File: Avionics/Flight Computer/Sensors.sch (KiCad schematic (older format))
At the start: 11 parts, among them U5 MPU-9250, U7 LPS25HB

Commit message: Finished routing and DRC check.
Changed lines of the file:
@@
 $EndComp
 $Comp
-L GND #PWR0106
+L GND #PWR0122
 U 1 1 58B4AF5E
 P 2400 5300
-F 0 "#PWR0106" H -1950 1500 50  0001 C CNN
+F 0 "#PWR0122" H -1950 1500 50  0001 C CNN
 F 1 "GND" H 2405 5127 50  0000 C CNN
 F 2 "" H -1950 1750 50  0001 C CNN
@@
 $EndComp
 $Comp
-L +3.3V #PWR0107
+L +3.3V #PWR0123
 U 1 1 58B4AFA2
 P 2300 2850
-F 0 "#PWR0107" H -2200 -700 50  0001 C CNN
+F 0 "#PWR0123" H -2200 -700 50  0001 C CNN
 F 1 "+3.3V" H 2315 3023 50  0000 C CNN
 F 2 "" H -2200 -550 50  0001 C CNN
@@
 $EndComp
 $Comp
-L GND #PWR0108
+L GND #PWR0124
 U 1 1 58B4B105
 P 8400 3550
-F 0 "#PWR0108" H 4050 -250 50  0001 C CNN
+F 0 "#PWR0124" H 4050 -250 50  0001 C CNN
 F 1 "GND" H 8405 3377 50  0000 C CNN
 F 2 "" H 4050 0   50  0001 C CNN
@@
 Connection ~ 8400 3550
 $Comp
-L +3.3V #PWR0109
+L +3.3V #PWR0125
 U 1 1 58B4B14B
 P 8450 1900
-F 0 "#PWR0109" H 3950 -1650 50  0001 C CNN
+F 0 "#PWR0125" H 3950 -1650 50  0001 C CNN
 F 1 "+3.3V" H 8465 2073 50  0000 C CNN
 F 2 "" H 3950 -1500 50  0001 C CNN
@@
 Connection ~ 8450 2350
 $Comp
-L GND #PWR0110
+L GND #PWR0126
 U 1 1 58B4B9E9
 P 9050 2700
-F 0 "#PWR0110" H 4700 -1100 50  0001 C CNN
+F 0 "#PWR0126" H 4700 -1100 50  0001 C CNN
 F 1 "GND" H 9055 2527 50  0000 C CNN
 F 2 "" H 4700 -850 50  0001 C CNN
@@
 Wire Wire Line
 	8450 2250 8450 2350
-Text Notes 8750 2150 0    60   ~ 0
+Text Notes 8750 2000 0    60   ~ 0
 Input filter to reduce sensor reference noise. \n1.5kHz cutoff, 25uA bias current worst case
 $Comp
-L +3.3V #PWR0111
+L +3.3V #PWR0127
 U 1 1 58B4C158
 P 7450 2100
-F 0 "#PWR0111" H 2950 -1450 50  0001 C CNN
+F 0 "#PWR0127" H 2950 -1450 50  0001 C CNN
 F 1 "+3.3V" H 7465 2273 50  0000 C CNN
 F 2 "" H 2950 -1300 50  0001 C CNN
@@
 	3100 4500 3850 4500
 $Comp
-L GND #PWR0112
+L GND #PWR0128
 U 1 1 58B4FB3E
 P 3850 4800
-F 0 "#PWR0112" H -500 1000 50  0001 C CNN
+F 0 "#PWR0128" H -500 1000 50  0001 C CNN
 F 1 "GND" H 3855 4627 50  0000 C CNN
 F 2 "" H -500 1250 50  0001 C CNN
@@
 	3500 4800 3500 4750
 $Comp
-L +3.3V #PWR0113
+L +3.3V #PWR0129
 U 1 1 58B50137
 P 3500 4750
-F 0 "#PWR0113" H -1000 1200 50  0001 C CNN
+F 0 "#PWR0129" H -1000 1200 50  0001 C CNN
 F 1 "+3.3V" H 3515 4923 50  0000 C CNN
 F 2 "" H -1000 1350 50  0001 C CNN
@@
 IMU-INT
 $Comp
-L GND #PWR0114
+L GND #PWR0130
 U 1 1 58B505FC
 P 3350 3600
-F 0 "#PWR0114" H -1000 -200 50  0001 C CNN
+F 0 "#PWR0130" H -1000 -200 50  0001 C CNN
 F 1 "GND" H 3355 3427 50  0000 C CNN
 F 2 "" H -1000 50  50  0001 C CNN
@@
 	2500 3300 3350 3300
 Connection ~ 2500 3300
-Text Notes 2800 3150 0    60   ~ 0
+Text Notes 2600 2800 0    60   ~ 0
 Input filter to reduce sensor reference noise. \n33kHz cutoff, 3.5mA bias current worst case
 $Comp
-L GND #PWR0115
+L GND #PWR0131
 U 1 1 58B50B96
 P 1500 3600
-F 0 "#PWR0115" H -2850 -200 50  0001 C CNN
+F 0 "#PWR0131" H -2850 -200 50  0001 C CNN
 F 1 "GND" H 1505 3427 50  0000 C CNN
 F 2 "" H -2850 50  50  0001 C CNN
@@
 	8300 3550 8500 3550
 NoConn ~ 8000 3200
+$Comp
+L PWR_FLAG #FLG0132
+U 1 1 58BF1DC3
+P 3050 3300
+F 0 "#FLG0132" H -1800 125 50  0001 C CNN
+F 1 "PWR_FLAG" H 3050 3474 50  0000 C CNN
+F 2 "" H -1800 50  50  0001 C CNN
+F 3 "" H -1800 50  50  0001 C CNN
+	1    3050 3300
+	1    0    0    -1
+$EndComp
+Connection ~ 3050 3300
+$Comp
+L PWR_FLAG #FLG0133
+U 1 1 58BF1E5B
+P 8900 2350
+F 0 "#FLG0133" H 4050 -825 50  0001 C CNN
+F 1 "PWR_FLAG" H 8900 2524 50  0000 C CNN
+F 2 "" H 4050 -900 50  0001 C CNN
+F 3 "" H 4050 -900 50  0001 C CNN
+	1    8900 2350
+	1    0    0    -1
+$EndComp
+Connection ~ 8900 2350
 $EndSCHEMATC

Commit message: Added LEDs
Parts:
- removed U7: LPS25HB, Housings_LGA:HLGA-10L_2.5x2.5mm_Pitch0.6mm, symbol LPS25HB-RESCUE-Flight_Computer
- added U7: LPS25HB, Housings_LGA:HLGA-10L_2.5x2.5mm_Pitch0.6mm, symbol LPS25HB
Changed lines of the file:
@@
 EESchema Schematic File Version 2
-LIBS:Flight Computer-rescue
 LIBS:device
 LIBS:rfcom
@@
 $EndComp
 $Comp
-L GND #PWR0122
+L GND #PWR0130
 U 1 1 58B4AF5E
 P 2400 5300
-F 0 "#PWR0122" H -1950 1500 50  0001 C CNN
+F 0 "#PWR0130" H -1950 1500 50  0001 C CNN
 F 1 "GND" H 2405 5127 50  0000 C CNN
 F 2 "" H -1950 1750 50  0001 C CNN
@@
 $EndComp
 $Comp
-L +3.3V #PWR0123
+L +3.3V #PWR0131
 U 1 1 58B4AFA2
 P 2300 2850
-F 0 "#PWR0123" H -2200 -700 50  0001 C CNN
+F 0 "#PWR0131" H -2200 -700 50  0001 C CNN
 F 1 "+3.3V" H 2315 3023 50  0000 C CNN
 F 2 "" H -2200 -550 50  0001 C CNN
@@
 $EndComp
 $Comp
-L GND #PWR0124
+L GND #PWR0132
 U 1 1 58B4B105
 P 8400 3550
-F 0 "#PWR0124" H 4050 -250 50  0001 C CNN
+F 0 "#PWR0132" H 4050 -250 50  0001 C CNN
 F 1 "GND" H 8405 3377 50  0000 C CNN
 F 2 "" H 4050 0   50  0001 C CNN
@@
 Connection ~ 8400 3550
 $Comp
-L +3.3V #PWR0125
+L +3.3V #PWR0133
 U 1 1 58B4B14B
 P 8450 1900
-F 0 "#PWR0125" H 3950 -1650 50  0001 C CNN
+F 0 "#PWR0133" H 3950 -1650 50  0001 C CNN
 F 1 "+3.3V" H 8465 2073 50  0000 C CNN
 F 2 "" H 3950 -1500 50  0001 C CNN
@@
 Connection ~ 8450 2350
 $Comp
-L GND #PWR0126
+L GND #PWR0134
 U 1 1 58B4B9E9
 P 9050 2700
-F 0 "#PWR0126" H 4700 -1100 50  0001 C CNN
+F 0 "#PWR0134" H 4700 -1100 50  0001 C CNN
 F 1 "GND" H 9055 2527 50  0000 C CNN
 F 2 "" H 4700 -850 50  0001 C CNN
@@
 Input filter to reduce sensor reference noise. \n1.5kHz cutoff, 25uA bias current worst case
 $Comp
-L +3.3V #PWR0127
+L +3.3V #PWR0135
 U 1 1 58B4C158
 P 7450 2100
-F 0 "#PWR0127" H 2950 -1450 50  0001 C CNN
+F 0 "#PWR0135" H 2950 -1450 50  0001 C CNN
 F 1 "+3.3V" H 7465 2273 50  0000 C CNN
 F 2 "" H 2950 -1300 50  0001 C CNN
@@
 	3100 4500 3850 4500
 $Comp
-L GND #PWR0128
+L GND #PWR0136
 U 1 1 58B4FB3E
 P 3850 4800
-F 0 "#PWR0128" H -500 1000 50  0001 C CNN
+F 0 "#PWR0136" H -500 1000 50  0001 C CNN
 F 1 "GND" H 3855 4627 50  0000 C CNN
 F 2 "" H -500 1250 50  0001 C CNN
@@
 	3500 4800 3500 4750
 $Comp
-L +3.3V #PWR0129
+L +3.3V #PWR0137
 U 1 1 58B50137
 P 3500 4750
-F 0 "#PWR0129" H -1000 1200 50  0001 C CNN
+F 0 "#PWR0137" H -1000 1200 50  0001 C CNN
 F 1 "+3.3V" H 3515 4923 50  0000 C CNN
 F 2 "" H -1000 1350 50  0001 C CNN
@@
 IMU-INT
 $Comp
-L GND #PWR0130
+L GND #PWR0138
 U 1 1 58B505FC
 P 3350 3600
-F 0 "#PWR0130" H -1000 -200 50  0001 C CNN
+F 0 "#PWR0138" H -1000 -200 50  0001 C CNN
 F 1 "GND" H 3355 3427 50  0000 C CNN
 F 2 "" H -1000 50  50  0001 C CNN
@@
 Input filter to reduce sensor reference noise. \n33kHz cutoff, 3.5mA bias current worst case
 $Comp
-L GND #PWR0131
+L GND #PWR0139
 U 1 1 58B50B96
 P 1500 3600
-F 0 "#PWR0131" H -2850 -200 50  0001 C CNN
+F 0 "#PWR0139" H -2850 -200 50  0001 C CNN
 F 1 "GND" H 1505 3427 50  0000 C CNN
 F 2 "" H -2850 50  50  0001 C CNN
@@
 Text Notes 3900 4100 0    60   ~ 0
 AUX bus goes to connector for expansion sensors
-$Comp
-L LPS25HB-RESCUE-Flight_Computer U7
-U 1 1 58B3E15F
-P 8400 2950
-AR Path="/58B3E15F" Ref="U7"  Part="1"
-AR Path="/58AA09D0/58B3E15F" Ref="U7"  Part="1"
-F 0 "U7" H 8071 2996 50  0000 R CNN
-F 1 "LPS25HB" H 8071 2905 50  0000 R CNN
-F 2 "Housings_LGA:HLGA-10L_2.5x2.5mm_Pitch0.6mm" H -1250 700 50  0001 C CIN
-F 3 "http://www.st.com/resource/en/datasheet/lps25hb.pdf" H -1250 800 50  0001 C CNN
-	1    8400 2950
-	-1   0    0    -1
-$EndComp
 Text Notes 1000 5900 0    60   ~ 0
 Layout Note: Exposed pad is NC. Do not solder the exposed pad.
 Wire Wire Line
-	8300 3550 8500 3550
+	8300 3550 8600 3550
 NoConn ~ 8000 3200
 $Comp
-L PWR_FLAG #FLG0132
+L PWR_FLAG #FLG0140
 U 1 1 58BF1DC3
 P 3050 3300
-F 0 "#FLG0132" H -1800 125 50  0001 C CNN
+F 0 "#FLG0140" H -1800 125 50  0001 C CNN
 F 1 "PWR_FLAG" H 3050 3474 50  0000 C CNN
 F 2 "" H -1800 50  50  0001 C CNN
@@
 Connection ~ 3050 3300
 $Comp
-L PWR_FLAG #FLG0133
+L PWR_FLAG #FLG0141
 U 1 1 58BF1E5B
 P 8900 2350
-F 0 "#FLG0133" H 4050 -825 50  0001 C CNN
+F 0 "#FLG0141" H 4050 -825 50  0001 C CNN
 F 1 "PWR_FLAG" H 8900 2524 50  0000 C CNN
 F 2 "" H 4050 -900 50  0001 C CNN
@@
 $EndComp
 Connection ~ 8900 2350
+$Comp
+L LPS25HB U7
+U 1 1 58BE66D3
+P 8400 2950
+F 0 "U7" H 8071 2996 50  0000 R CNN
+F 1 "LPS25HB" H 8071 2905 50  0000 R CNN
+F 2 "Housings_LGA:HLGA-10L_2.5x2.5mm_Pitch0.6mm" H -1250 1100 50  0001 C CIN
+F 3 "http://www.st.com/resource/en/datasheet/lps25hb.pdf" H -1250 1200 50  0001 C CNN
+	1    8400 2950
+	-1   0    0    -1
+$EndComp
+Connection ~ 8500 3550
 $EndSCHEMATC

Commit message: Changed LED configuration, added smart driver chip to let all the CPUs access it..
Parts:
- C54, C55, C56, C58, R15, R16, R17, R18, R19: Voltage 50V -> 16V
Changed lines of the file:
@@
 $EndComp
 $Comp
-L GND #PWR0130
+L GND #PWR0134
 U 1 1 58B4AF5E
 P 2400 5300
-F 0 "#PWR0130" H -1950 1500 50  0001 C CNN
+F 0 "#PWR0134" H -1950 1500 50  0001 C CNN
 F 1 "GND" H 2405 5127 50  0000 C CNN
 F 2 "" H -1950 1750 50  0001 C CNN
@@
 $EndComp
 $Comp
-L +3.3V #PWR0131
+L +3.3V #PWR0135
 U 1 1 58B4AFA2
 P 2300 2850
-F 0 "#PWR0131" H -2200 -700 50  0001 C CNN
+F 0 "#PWR0135" H -2200 -700 50  0001 C CNN
 F 1 "+3.3V" H 2315 3023 50  0000 C CNN
 F 2 "" H -2200 -550 50  0001 C CNN
@@
 $EndComp
 $Comp
-L GND #PWR0132
+L GND #PWR0136
 U 1 1 58B4B105
 P 8400 3550
-F 0 "#PWR0132" H 4050 -250 50  0001 C CNN
+F 0 "#PWR0136" H 4050 -250 50  0001 C CNN
 F 1 "GND" H 8405 3377 50  0000 C CNN
 F 2 "" H 4050 0   50  0001 C CNN
@@
 Connection ~ 8400 3550
 $Comp
-L +3.3V #PWR0133
+L +3.3V #PWR0137
 U 1 1 58B4B14B
 P 8450 1900
-F 0 "#PWR0133" H 3950 -1650 50  0001 C CNN
+F 0 "#PWR0137" H 3950 -1650 50  0001 C CNN
 F 1 "+3.3V" H 8465 2073 50  0000 C CNN
 F 2 "" H 3950 -1500 50  0001 C CNN
@@
 F 2 "Capacitors_SMD:C_0402" H 2288 -1350 50  0001 C CNN
 F 3 "" H 2250 -1200 50  0001 C CNN
-F 4 "50V" H 2350 -1250 60  0001 L CNN "Voltage"
+F 4 "16V" H 2350 -1250 60  0001 L CNN "Voltage"
 F 5 "20%" H 2350 -1150 60  0001 L CNN "Tolerance"
 F 6 "X7R" H 2300 -1050 60  0001 L CNN "Type"
@@
 Connection ~ 8450 2350
 $Comp
-L GND #PWR0134
+L GND #PWR0138
 U 1 1 58B4B9E9
 P 9050 2700
-F 0 "#PWR0134" H 4700 -1100 50  0001 C CNN
+F 0 "#PWR0138" H 4700 -1100 50  0001 C CNN
 F 1 "GND" H 9055 2527 50  0000 C CNN
 F 2 "" H 4700 -850 50  0001 C CNN
@@
 F 3 "" V 1280 450 50  0001 C CNN
 F 4 "1%" H 8520 2009 60  0000 L CNN "Tolerance"
-F 5 "50V" V 1450 450 60  0001 C CNN "Voltage"
+F 5 "16V" V 1450 450 60  0001 C CNN "Voltage"
 F 6 "0.062W" V 1550 450 60  0001 C CNN "Power"
 F 7 "Thin Film" V 1650 450 60  0001 C CNN "Material"
@@
 Input filter to reduce sensor reference noise. \n1.5kHz cutoff, 25uA bias current worst case
 $Comp
-L +3.3V #PWR0135
+L +3.3V #PWR0139
 U 1 1 58B4C158
 P 7450 2100
-F 0 "#PWR0135" H 2950 -1450 50  0001 C CNN
+F 0 "#PWR0139" H 2950 -1450 50  0001 C CNN
 F 1 "+3.3V" H 7465 2273 50  0000 C CNN
 F 2 "" H 2950 -1300 50  0001 C CNN
@@
 F 3 "" V 280 700 50  0001 C CNN
 F 4 "1%" H 7520 2259 60  0000 L CNN "Tolerance"
-F 5 "50V" V 450 700 60  0001 C CNN "Voltage"
+F 5 "16V" V 450 700 60  0001 C CNN "Voltage"
 F 6 "0.062W" V 550 700 60  0001 C CNN "Power"
 F 7 "Thin Film" V 650 700 60  0001 C CNN "Material"
@@
 F 3 "" V 30  700 50  0001 C CNN
 F 4 "1%" H 7270 2259 60  0000 L CNN "Tolerance"
-F 5 "50V" V 200 700 60  0001 C CNN "Voltage"
+F 5 "16V" V 200 700 60  0001 C CNN "Voltage"
 F 6 "0.062W" V 300 700 60  0001 C CNN "Power"
 F 7 "Thin Film" V 400 700 60  0001 C CNN "Material"
@@
 F 3 "" V -220 700 50  0001 C CNN
 F 4 "1%" H 7020 2259 60  0000 L CNN "Tolerance"
-F 5 "50V" V -50 700 60  0001 C CNN "Voltage"
+F 5 "16V" V -50 700 60  0001 C CNN "Voltage"
 F 6 "0.062W" V 50  700 60  0001 C CNN "Power"
 F 7 "Thin Film" V 150 700 60  0001 C CNN "Material"
@@
 F 3 "" V -520 1650 50  0001 C CNN
 F 4 "1%" H 2570 3009 60  0000 L CNN "Tolerance"
-F 5 "50V" V -350 1650 60  0001 C CNN "Voltage"
+F 5 "16V" V -350 1650 60  0001 C CNN "Voltage"
 F 6 "0.062W" V -250 1650 60  0001 C CNN "Power"
 F 7 "Thin Film" V -150 1650 60  0001 C CNN "Material"
@@
 F 2 "Capacitors_SMD:C_0402" H -3412 -450 50  0001 C CNN
 F 3 "" H -3450 -300 50  0001 C CNN
-F 4 "50V" H -3350 -350 60  0001 L CNN "Voltage"
+F 4 "16V" H -3350 -350 60  0001 L CNN "Voltage"
 F 5 "20%" H -3350 -250 60  0001 L CNN "Tolerance"
 F 6 "X7R" H -3400 -150 60  0001 L CNN "Type"
@@
 F 2 "Capacitors_SMD:C_0402" H -5262 -450 50  0001 C CNN
 F 3 "" H -5300 -300 50  0001 C CNN
-F 4 "50V" H -5200 -350 60  0001 L CNN "Voltage"
+F 4 "16V" H -5200 -350 60  0001 L CNN "Voltage"
 F 5 "20%" H -5200 -250 60  0001 L CNN "Tolerance"
 F 6 "X7R" H -5250 -150 60  0001 L CNN "Type"
@@
 F 2 "Capacitors_SMD:C_0402" H -2912 750 50  0001 C CNN
 F 3 "" H -2950 900 50  0001 C CNN
-F 4 "50V" H -2850 850 60  0001 L CNN "Voltage"
+F 4 "16V" H -2850 850 60  0001 L CNN "Voltage"
 F 5 "20%" H -2850 950 60  0001 L CNN "Tolerance"
 F 6 "X7R" H -2900 1050 60  0001 L CNN "Type"
@@
 	3100 4500 3850 4500
 $Comp
-L GND #PWR0136
+L GND #PWR0140
 U 1 1 58B4FB3E
 P 3850 4800
-F 0 "#PWR0136" H -500 1000 50  0001 C CNN
+F 0 "#PWR0140" H -500 1000 50  0001 C CNN
 F 1 "GND" H 3855 4627 50  0000 C CNN
 F 2 "" H -500 1250 50  0001 C CNN
@@
 	3500 4800 3500 4750
 $Comp
-L +3.3V #PWR0137
+L +3.3V #PWR0141
 U 1 1 58B50137
 P 3500 4750
-F 0 "#PWR0137" H -1000 1200 50  0001 C CNN
+F 0 "#PWR0141" H -1000 1200 50  0001 C CNN
 F 1 "+3.3V" H 3515 4923 50  0000 C CNN
 F 2 "" H -1000 1350 50  0001 C CNN
@@
 IMU-INT
 $Comp
-L GND #PWR0138
+L GND #PWR0142
 U 1 1 58B505FC
 P 3350 3600
-F 0 "#PWR0138" H -1000 -200 50  0001 C CNN
+F 0 "#PWR0142" H -1000 -200 50  0001 C CNN
 F 1 "GND" H 3355 3427 50  0000 C CNN
 F 2 "" H -1000 50  50  0001 C CNN
@@
 Input filter to reduce sensor reference noise. \n33kHz cutoff, 3.5mA bias current worst case
 $Comp
-L GND #PWR0139
+L GND #PWR0143
 U 1 1 58B50B96
 P 1500 3600
-F 0 "#PWR0139" H -2850 -200 50  0001 C CNN
+F 0 "#PWR0143" H -2850 -200 50  0001 C CNN
 F 1 "GND" H 1505 3427 50  0000 C CNN
 F 2 "" H -2850 50  50  0001 C CNN
@@
 NoConn ~ 8000 3200
 $Comp
-L PWR_FLAG #FLG0140
+L PWR_FLAG #FLG0144
 U 1 1 58BF1DC3
 P 3050 3300
-F 0 "#FLG0140" H -1800 125 50  0001 C CNN
+F 0 "#FLG0144" H -1800 125 50  0001 C CNN
 F 1 "PWR_FLAG" H 3050 3474 50  0000 C CNN
 F 2 "" H -1800 50  50  0001 C CNN
@@
 Connection ~ 3050 3300
 $Comp
-L PWR_FLAG #FLG0141
+L PWR_FLAG #FLG0145
 U 1 1 58BF1E5B
 P 8900 2350
-F 0 "#FLG0141" H 4050 -825 50  0001 C CNN
+F 0 "#FLG0145" H 4050 -825 50  0001 C CNN
 F 1 "PWR_FLAG" H 8900 2524 50  0000 C CNN
 F 2 "" H 4050 -900 50  0001 C CNN

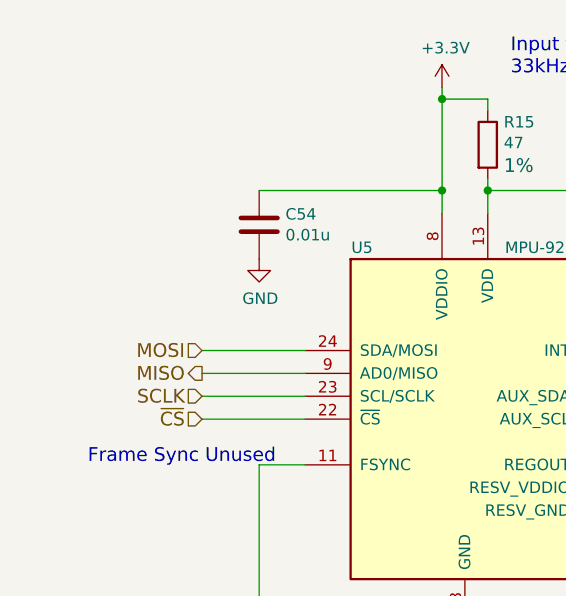
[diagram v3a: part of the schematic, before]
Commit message: Added pullup to CS
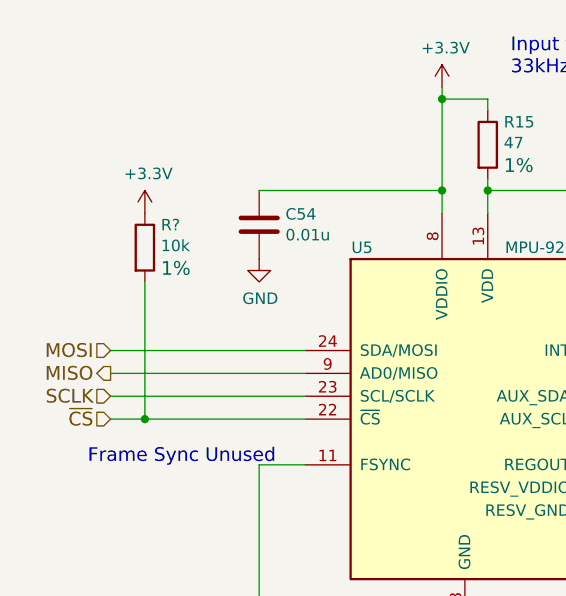
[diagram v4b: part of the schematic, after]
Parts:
- added R?: 10k, Resistors_SMD:R_0402, symbol R
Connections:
- net +3V3: now also R?.1
- net ~CS: now also R?.2
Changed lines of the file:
@@
 $EndComp
 $Comp
-L GND #PWR0134
+L GND #PWR120
 U 1 1 58B4AF5E
 P 2400 5300
-F 0 "#PWR0134" H -1950 1500 50  0001 C CNN
+F 0 "#PWR120" H -1950 1500 50  0001 C CNN
 F 1 "GND" H 2405 5127 50  0000 C CNN
 F 2 "" H -1950 1750 50  0001 C CNN
@@
 $EndComp
 $Comp
-L +3.3V #PWR0135
+L +3.3V #PWR119
 U 1 1 58B4AFA2
 P 2300 2850
-F 0 "#PWR0135" H -2200 -700 50  0001 C CNN
+F 0 "#PWR119" H -2200 -700 50  0001 C CNN
 F 1 "+3.3V" H 2315 3023 50  0000 C CNN
 F 2 "" H -2200 -550 50  0001 C CNN
@@
 $EndComp
 $Comp
-L GND #PWR0136
+L GND #PWR125
 U 1 1 58B4B105
 P 8400 3550
-F 0 "#PWR0136" H 4050 -250 50  0001 C CNN
+F 0 "#PWR125" H 4050 -250 50  0001 C CNN
 F 1 "GND" H 8405 3377 50  0000 C CNN
 F 2 "" H 4050 0   50  0001 C CNN
@@
 Connection ~ 8400 3550
 $Comp
-L +3.3V #PWR0137
+L +3.3V #PWR126
 U 1 1 58B4B14B
 P 8450 1900
-F 0 "#PWR0137" H 3950 -1650 50  0001 C CNN
+F 0 "#PWR126" H 3950 -1650 50  0001 C CNN
 F 1 "+3.3V" H 8465 2073 50  0000 C CNN
 F 2 "" H 3950 -1500 50  0001 C CNN
@@
 Connection ~ 8450 2350
 $Comp
-L GND #PWR0138
+L GND #PWR127
 U 1 1 58B4B9E9
 P 9050 2700
-F 0 "#PWR0138" H 4700 -1100 50  0001 C CNN
+F 0 "#PWR127" H 4700 -1100 50  0001 C CNN
 F 1 "GND" H 9055 2527 50  0000 C CNN
 F 2 "" H 4700 -850 50  0001 C CNN
@@
 Input filter to reduce sensor reference noise. \n1.5kHz cutoff, 25uA bias current worst case
 $Comp
-L +3.3V #PWR0139
+L +3.3V #PWR124
 U 1 1 58B4C158
 P 7450 2100
-F 0 "#PWR0139" H 2950 -1450 50  0001 C CNN
+F 0 "#PWR124" H 2950 -1450 50  0001 C CNN
 F 1 "+3.3V" H 7465 2273 50  0000 C CNN
 F 2 "" H 2950 -1300 50  0001 C CNN
@@
 Text Notes 1800 5650 0    60   ~ 0
 9-DOF IMU, gyro/accel/mag
-Text HLabel 1250 4300 0    60   Input ~ 0
+Text HLabel 850  4300 0    60   Input ~ 0
 ~CS
 Wire Wire Line
-	1250 4300 1700 4300
-Wire Wire Line
-	1700 4200 1250 4200
-Wire Wire Line
-	1700 4100 1250 4100
-Wire Wire Line
-	1250 4000 1700 4000
-Text HLabel 1250 4200 0    60   Input ~ 0
+	850  4300 1700 4300
+Wire Wire Line
+	1700 4200 850  4200
+Wire Wire Line
+	1700 4100 850  4100
+Wire Wire Line
+	850  4000 1700 4000
+Text HLabel 850  4200 0    60   Input ~ 0
 SCLK
-Text HLabel 1250 4100 0    60   Output ~ 0
+Text HLabel 850  4100 0    60   Output ~ 0
 MISO
-Text HLabel 1250 4000 0    60   Input ~ 0
+Text HLabel 850  4000 0    60   Input ~ 0
 MOSI
 $Comp
@@
 	3100 4500 3850 4500
 $Comp
-L GND #PWR0140
+L GND #PWR123
 U 1 1 58B4FB3E
 P 3850 4800
-F 0 "#PWR0140" H -500 1000 50  0001 C CNN
+F 0 "#PWR123" H -500 1000 50  0001 C CNN
 F 1 "GND" H 3855 4627 50  0000 C CNN
 F 2 "" H -500 1250 50  0001 C CNN
@@
 	3500 4800 3500 4750
 $Comp
-L +3.3V #PWR0141
+L +3.3V #PWR122
 U 1 1 58B50137
 P 3500 4750
-F 0 "#PWR0141" H -1000 1200 50  0001 C CNN
+F 0 "#PWR122" H -1000 1200 50  0001 C CNN
 F 1 "+3.3V" H 3515 4923 50  0000 C CNN
 F 2 "" H -1000 1350 50  0001 C CNN
@@
 IMU-INT
 $Comp
-L GND #PWR0142
+L GND #PWR121
 U 1 1 58B505FC
 P 3350 3600
-F 0 "#PWR0142" H -1000 -200 50  0001 C CNN
+F 0 "#PWR121" H -1000 -200 50  0001 C CNN
 F 1 "GND" H 3355 3427 50  0000 C CNN
 F 2 "" H -1000 50  50  0001 C CNN
@@
 Input filter to reduce sensor reference noise. \n33kHz cutoff, 3.5mA bias current worst case
 $Comp
-L GND #PWR0143
+L GND #PWR118
 U 1 1 58B50B96
 P 1500 3600
-F 0 "#PWR0143" H -2850 -200 50  0001 C CNN
+F 0 "#PWR118" H -2850 -200 50  0001 C CNN
 F 1 "GND" H 1505 3427 50  0000 C CNN
 F 2 "" H -2850 50  50  0001 C CNN
@@
 NoConn ~ 8000 3200
 $Comp
-L PWR_FLAG #FLG0144
+L PWR_FLAG #FLG17
 U 1 1 58BF1DC3
 P 3050 3300
-F 0 "#FLG0144" H -1800 125 50  0001 C CNN
+F 0 "#FLG17" H -1800 125 50  0001 C CNN
 F 1 "PWR_FLAG" H 3050 3474 50  0000 C CNN
 F 2 "" H -1800 50  50  0001 C CNN
@@
 Connection ~ 3050 3300
 $Comp
-L PWR_FLAG #FLG0145
+L PWR_FLAG #FLG18
 U 1 1 58BF1E5B
 P 8900 2350
-F 0 "#FLG0145" H 4050 -825 50  0001 C CNN
+F 0 "#FLG18" H 4050 -825 50  0001 C CNN
 F 1 "PWR_FLAG" H 8900 2524 50  0000 C CNN
 F 2 "" H 4050 -900 50  0001 C CNN
@@
 $EndComp
 Connection ~ 8500 3550
+$Comp
+L R R?
+U 1 1 58D7F4C9
+P 1000 3550
+F 0 "R?" H 1070 3649 50  0000 L CNN
+F 1 "10k" H 1070 3558 50  0000 L CNN
+F 2 "Resistors_SMD:R_0402" V -6450 1900 50  0001 C CNN
+F 3 "" V -6170 1900 50  0001 C CNN
+F 4 "1%" H 1070 3459 60  0000 L CNN "Tolerance"
+F 5 "16V" V -6000 1900 60  0001 C CNN "Voltage"
+F 6 "0.062W" V -5900 1900 60  0001 C CNN "Power"
+F 7 "Thin Film" V -5800 1900 60  0001 C CNN "Material"
+F 8 "0402" V -6350 1900 60  0001 C CNN "Package"
+	1    1000 3550
+	1    0    0    -1
+$EndComp
+$Comp
+L +3.3V #PWR?
+U 1 1 58D7F763
+P 1000 3400
+F 0 "#PWR?" H -3500 -150 50  0001 C CNN
+F 1 "+3.3V" H 1015 3573 50  0000 C CNN
+F 2 "" H -3500 0   50  0001 C CNN
+F 3 "" H -3500 0   50  0001 C CNN
+	1    1000 3400
+	1    0    0    -1
+$EndComp
+Wire Wire Line
+	1000 3700 1000 4300
+Connection ~ 1000 4300
 $EndSCHEMATC
